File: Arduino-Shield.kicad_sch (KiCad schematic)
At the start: 15 parts, among them J1 Power, J2 Digital/PWM, J3 Analog, J4 Digital/PWM, J5 Conn_01x04_Pin, J6 Conn_01x04_Pin, J7 AudioJack4, U1 DHT11, U2 LM358

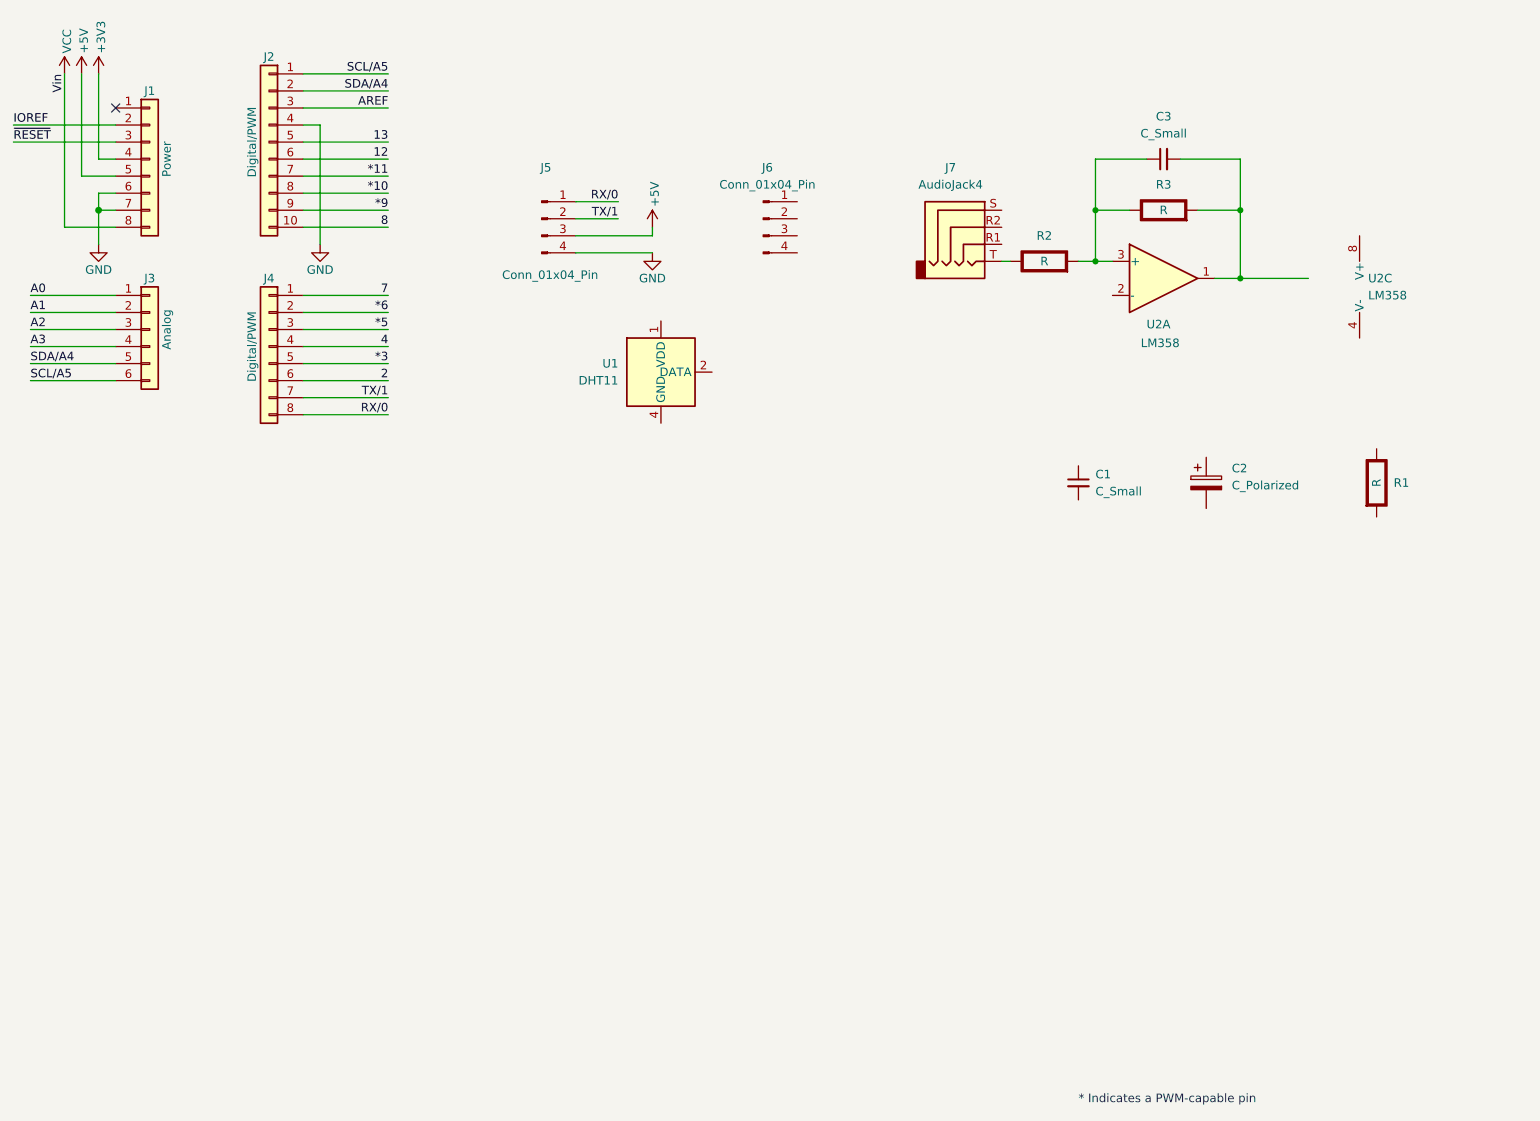
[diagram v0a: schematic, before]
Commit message: cambios en título y descripción del esquema y placa
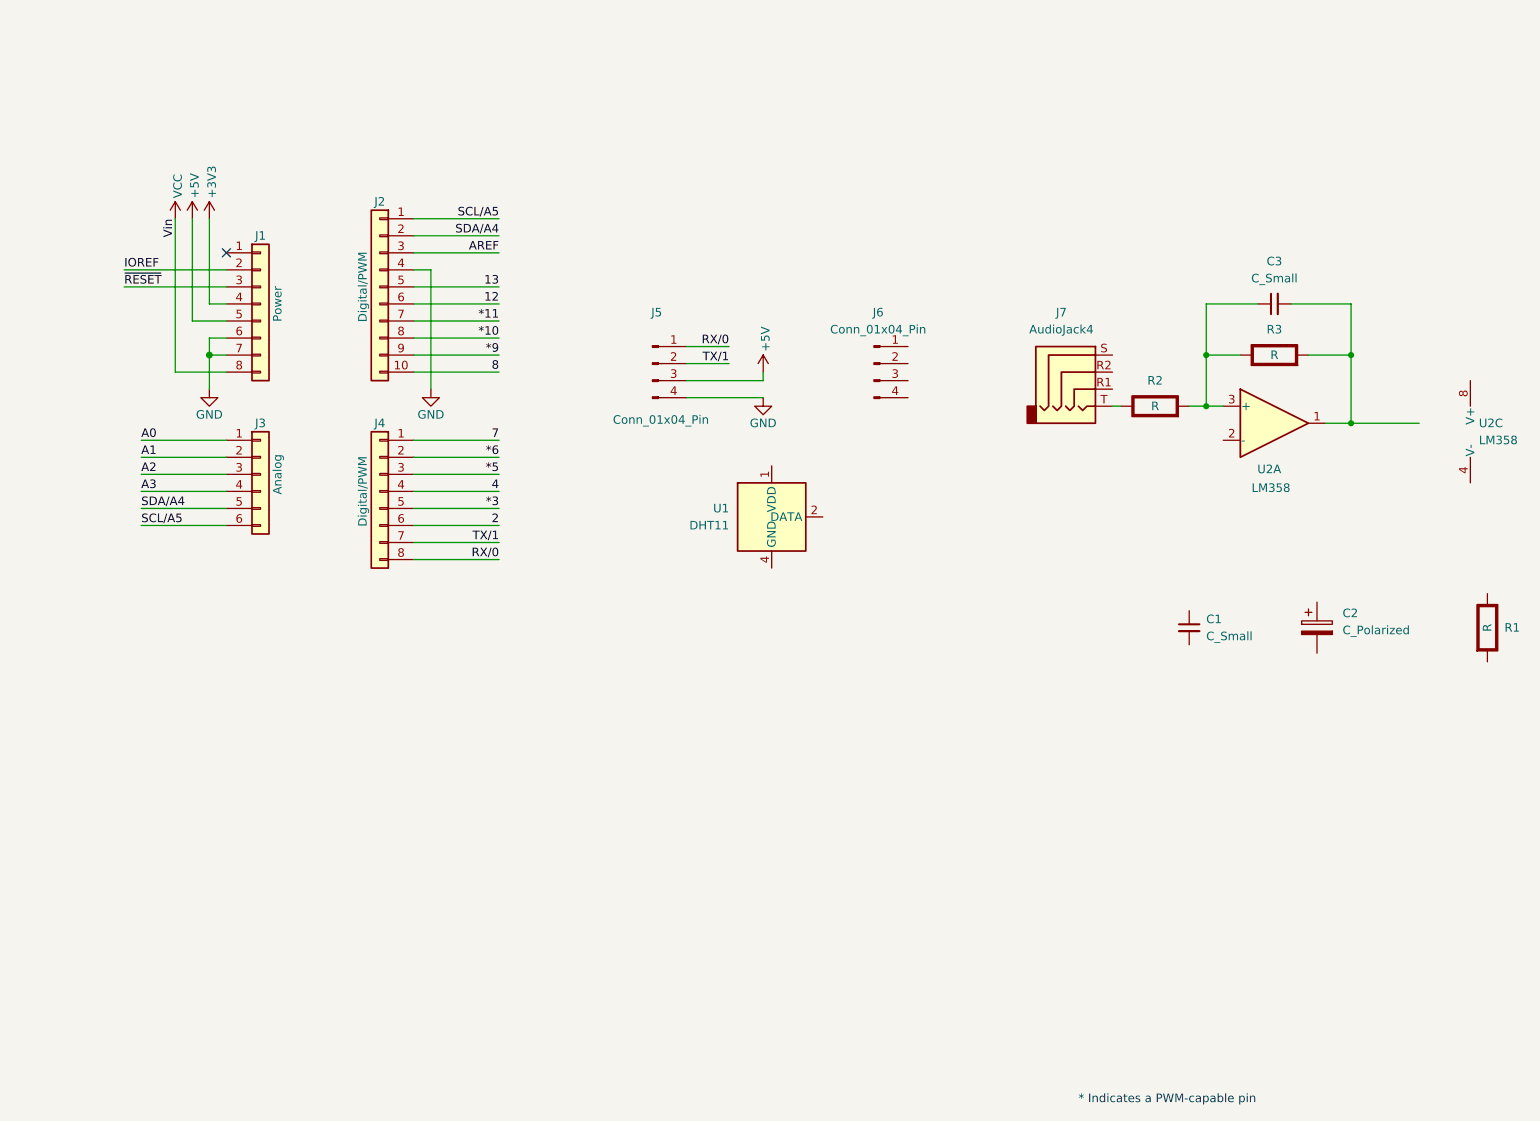
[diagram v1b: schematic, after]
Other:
- company: (none) -> Curso Lab. Electrónica II
- title: (none) -> Shield Arduino UNO
- moved on the sheet: C1, C2, C3, J1, J2, J3, J4, J5, J6, J7, R1, R2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
